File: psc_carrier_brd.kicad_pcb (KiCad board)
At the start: 2 copper layers, 12 parts, among them J1 Conn_01x08_Pin, J2 Conn_01x05_Pin - 3.3v, J3 Conn_01x05_Pin - 5v, J4 6469028-1, J5 39301022, U1 WeMos_D1_mini, U5 OPA2197xDGK

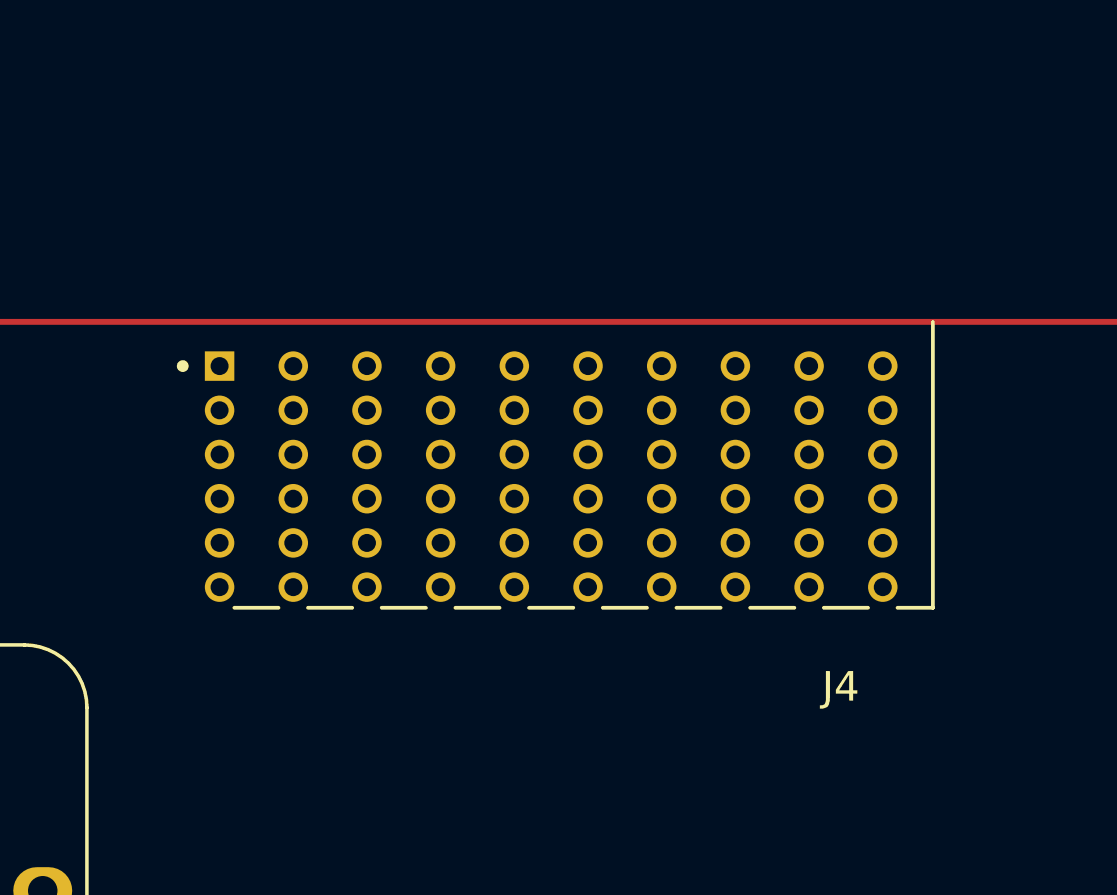
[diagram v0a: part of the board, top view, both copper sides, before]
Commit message: Create 6469028-1 symbol
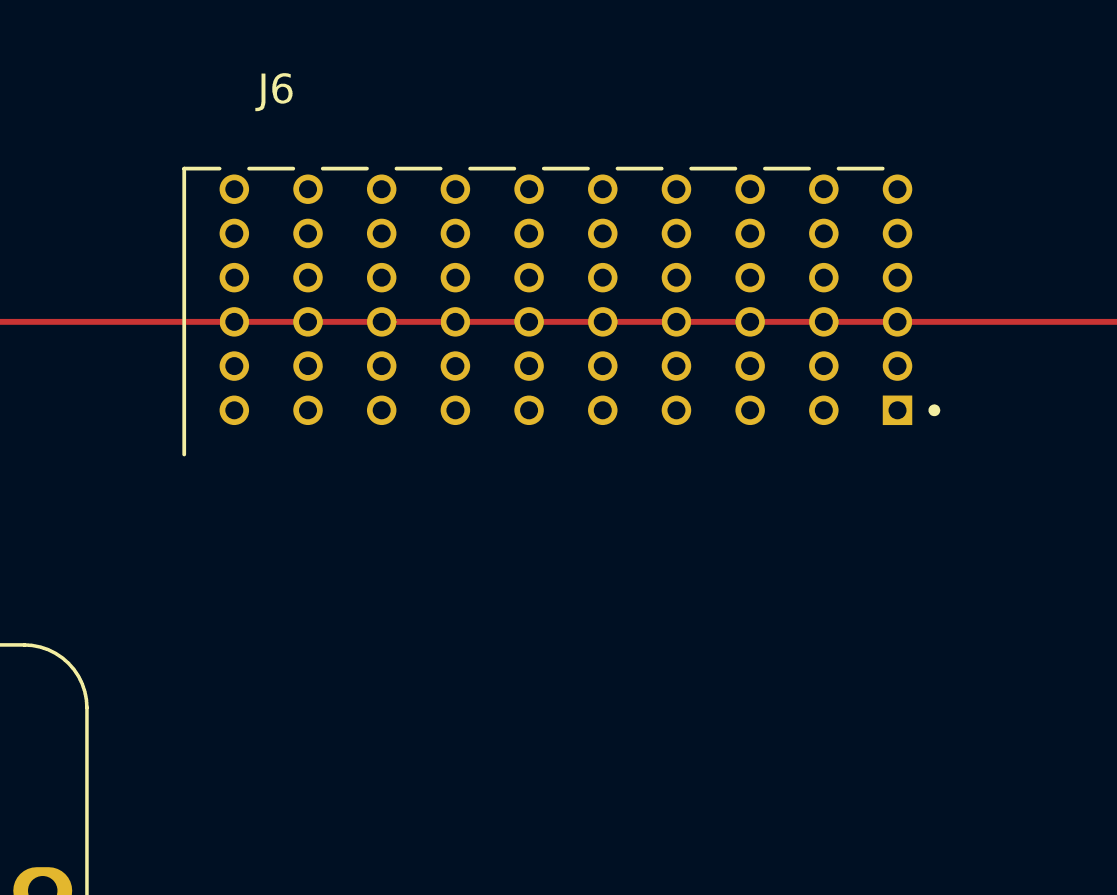
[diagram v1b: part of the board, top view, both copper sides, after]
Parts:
- removed J4: 6469028-1, myparts:TE_6469028-1
- added J6: 6469028-1, myparts:TE_6469028-1, F.Cu at (162.5, 53.0)

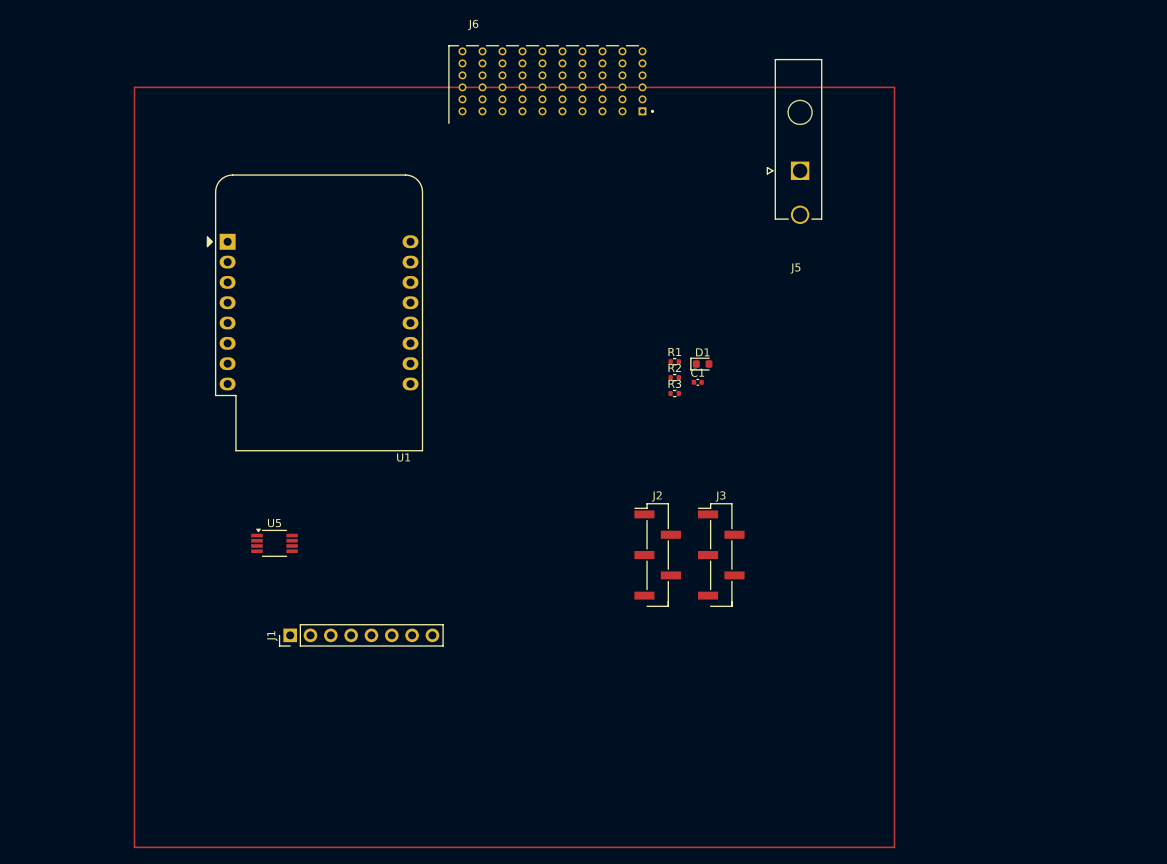
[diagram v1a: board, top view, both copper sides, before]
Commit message: Create custom NSLS2 worksheet
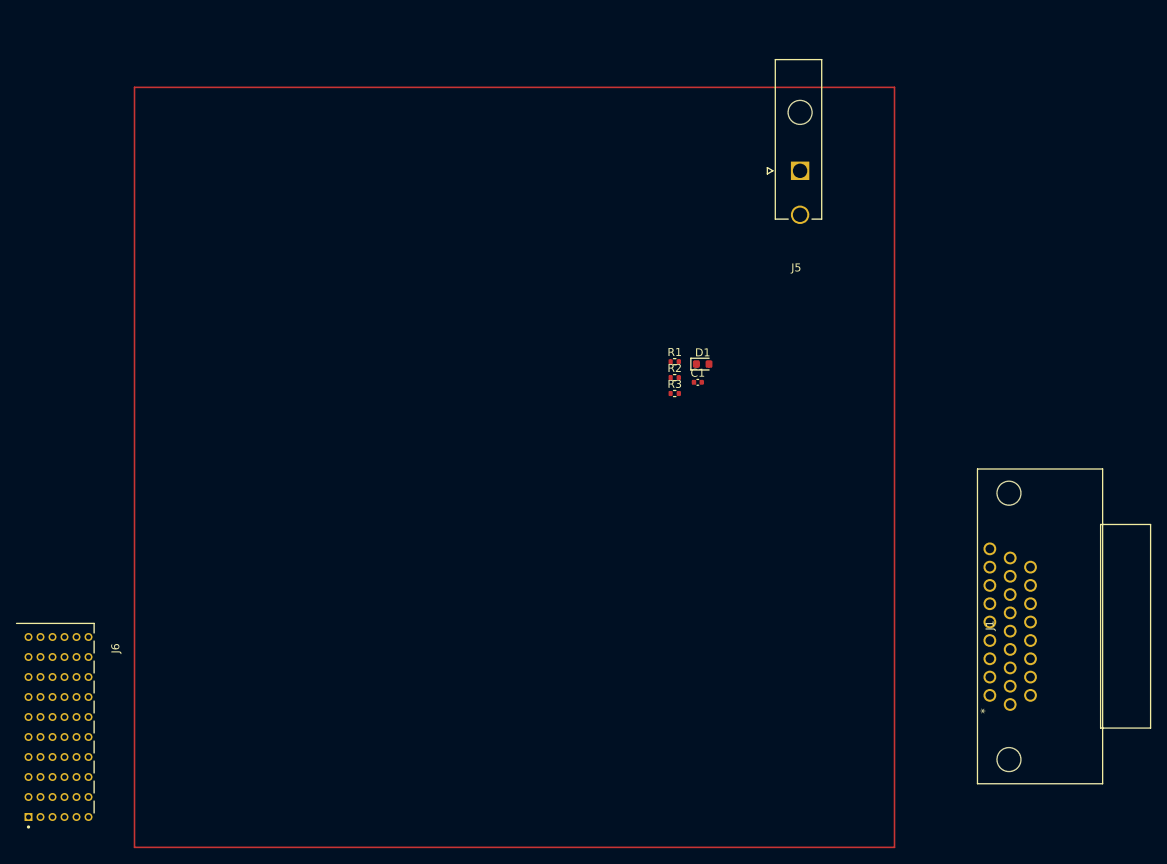
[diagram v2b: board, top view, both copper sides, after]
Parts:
- removed J2: Conn_01x05_Pin - 3.3v, Connector_PinHeader_2.54mm:PinHeader_1x05_P2.54mm_Vertical_SMD_Pin1Left
- removed J3: Conn_01x05_Pin - 5v, Connector_PinHeader_2.54mm:PinHeader_1x05_P2.54mm_Vertical_SMD_Pin1Left
- removed U1: WeMos_D1_mini, Module:WEMOS_D1_mini_light
- removed U5: OPA2197xDGK, Package_SO:VSSOP-8_3.0x3.0mm_P0.65mm
- J1: value Conn_01x08_Pin -> 1731130154; footprint Connector_PinHeader_2.54mm:PinHeader_1x08_P2.54mm_Vertical -> myparts:CONN_F15-26P135G0-5979_MOL
- moved J6 116.9 mm to (85.8, 141.2), turned to -90 degrees
- moved J1 87.8 mm to (205.9, 126.0), turned to -90 degrees
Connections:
- D1 pad 2: Net-(D1-A) -> unconnected-(D1-A-Pad2)
- J1 pad 1: Net-(D1-A) -> unconnected-(J1-Pad1)
- J1 pad 5: Net-(J1-Pin_5) -> unconnected-(J1-Pad5)
- J1 pad 7: Net-(J1-Pin_7) -> unconnected-(J1-Pad7)
- J1 pad 8: Net-(J1-Pin_8) -> unconnected-(J1-Pad8)
- J6 pad A10: (no net) -> unconnected-(J6-PadA10)
- J6 pad A2: (no net) -> unconnected-(J6-PadA2)
- J6 pad A3: (no net) -> unconnected-(J6-PadA3)
- J6 pad A4: (no net) -> unconnected-(J6-PadA4)
- J6 pad A5: (no net) -> unconnected-(J6-PadA5)
- J6 pad A6: (no net) -> unconnected-(J6-PadA6)
- J6 pad A7: (no net) -> unconnected-(J6-PadA7)
- J6 pad A8: (no net) -> unconnected-(J6-PadA8)
- J6 pad A9: (no net) -> unconnected-(J6-PadA9)
- J6 pad B10: (no net) -> unconnected-(J6-PadB10)
- J6 pad B2: (no net) -> unconnected-(J6-PadB2)
- J6 pad B3: (no net) -> unconnected-(J6-PadB3)
- J6 pad B4: (no net) -> unconnected-(J6-PadB4)
- J6 pad B5: (no net) -> unconnected-(J6-PadB5)
- J6 pad B6: (no net) -> unconnected-(J6-PadB6)
- J6 pad B7: (no net) -> unconnected-(J6-PadB7)
- J6 pad B8: (no net) -> unconnected-(J6-PadB8)
- J6 pad B9: (no net) -> unconnected-(J6-PadB9)
- J6 pad BG10: (no net) -> unconnected-(J6-PadBG10)
- J6 pad BG2: (no net) -> unconnected-(J6-PadBG2)
- J6 pad BG3: (no net) -> unconnected-(J6-PadBG3)
- J6 pad BG4: (no net) -> unconnected-(J6-PadBG4)
- J6 pad BG5: (no net) -> unconnected-(J6-PadBG5)
- J6 pad BG6: (no net) -> unconnected-(J6-PadBG6)
- J6 pad BG7: (no net) -> unconnected-(J6-PadBG7)
- J6 pad BG8: (no net) -> unconnected-(J6-PadBG8)
- J6 pad BG9: (no net) -> unconnected-(J6-PadBG9)
- J6 pad C10: (no net) -> unconnected-(J6-PadC10)
- J6 pad C2: (no net) -> unconnected-(J6-PadC2)
- J6 pad C3: (no net) -> unconnected-(J6-PadC3)
- J6 pad C4: (no net) -> unconnected-(J6-PadC4)
- J6 pad C5: (no net) -> unconnected-(J6-PadC5)
- J6 pad C6: (no net) -> unconnected-(J6-PadC6)
- J6 pad C7: (no net) -> unconnected-(J6-PadC7)
- J6 pad C8: (no net) -> unconnected-(J6-PadC8)
- J6 pad C9: (no net) -> unconnected-(J6-PadC9)
- J6 pad D10: (no net) -> unconnected-(J6-PadD10)
- J6 pad D2: (no net) -> unconnected-(J6-PadD2)
- J6 pad D3: (no net) -> unconnected-(J6-PadD3)
- J6 pad D4: (no net) -> unconnected-(J6-PadD4)
- J6 pad D5: (no net) -> unconnected-(J6-PadD5)
- J6 pad D6: (no net) -> unconnected-(J6-PadD6)
- J6 pad D7: (no net) -> unconnected-(J6-PadD7)
- J6 pad D8: (no net) -> unconnected-(J6-PadD8)
- J6 pad D9: (no net) -> unconnected-(J6-PadD9)
- J6 pad DG10: (no net) -> unconnected-(J6-PadDG10)
- J6 pad DG2: (no net) -> unconnected-(J6-PadDG2)
- J6 pad DG3: (no net) -> unconnected-(J6-PadDG3)
- J6 pad DG4: (no net) -> unconnected-(J6-PadDG4)
- J6 pad DG5: (no net) -> unconnected-(J6-PadDG5)
- J6 pad DG6: (no net) -> unconnected-(J6-PadDG6)
- J6 pad DG7: (no net) -> unconnected-(J6-PadDG7)
- J6 pad DG8: (no net) -> unconnected-(J6-PadDG8)
- J6 pad DG9: (no net) -> unconnected-(J6-PadDG9)

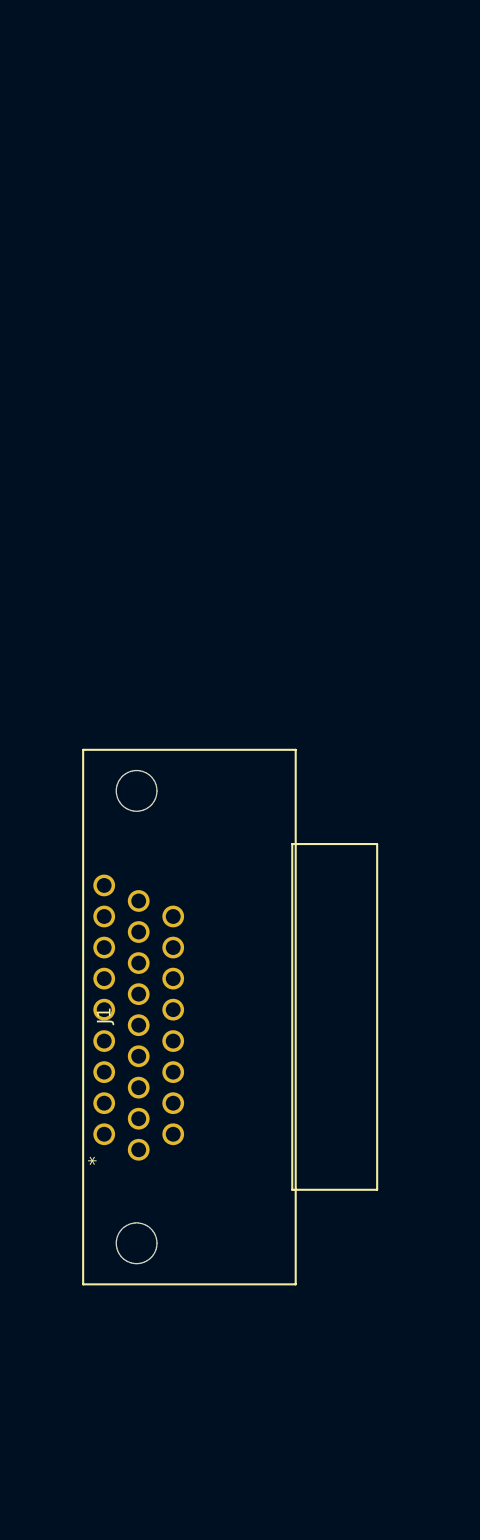
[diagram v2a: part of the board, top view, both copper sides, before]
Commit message: Add footprint for PS connector
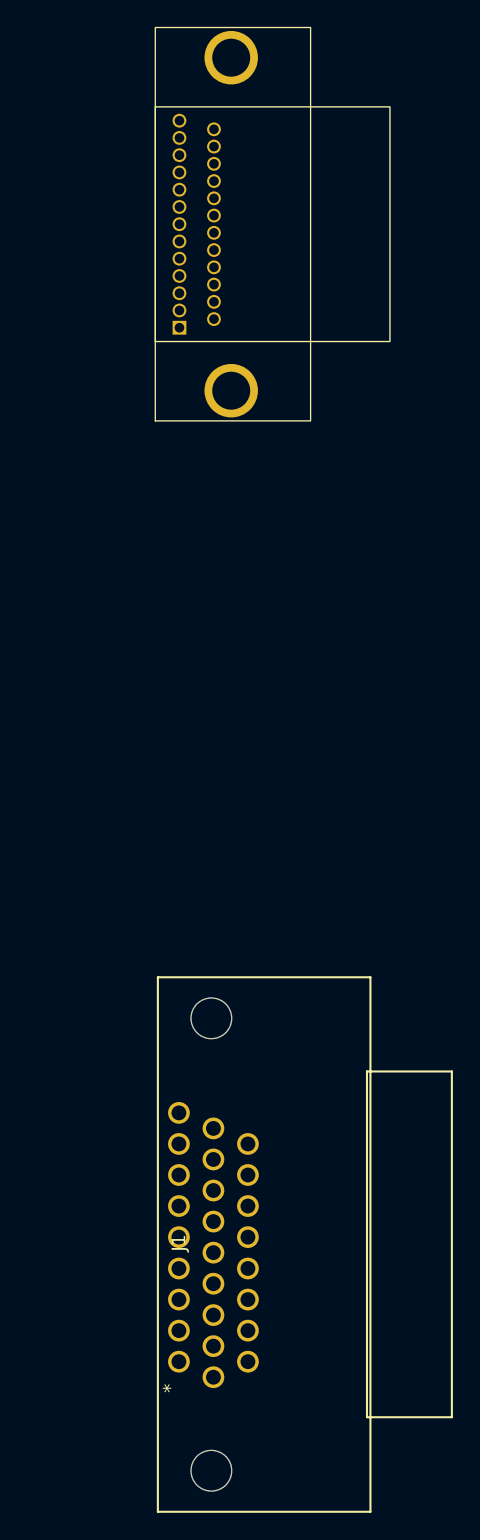
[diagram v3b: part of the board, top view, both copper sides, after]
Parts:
- added J2: 0836149012, myparts:0836149012, F.Cu at (211.5, 59.0)
- moved J1 17.6 mm to (211.4, 142.7)

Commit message: Add board outline
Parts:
- moved J2 135.5 mm to (76.2, 67.3), turned to 180 degrees
- moved J5 126.9 mm to (268.3, 153.7), turned to 90 degrees
- moved J6 87.0 mm to (132.0, 214.9), turned to 0 degrees
- moved J1 81.4 mm to (250.2, 71.1), turned to 0 degrees
- moved C1 50.3 mm to (200.6, 126.3)
- moved R2 50.3 mm to (197.7, 125.8)
- moved R3 50.3 mm to (197.7, 127.8)
- moved D1 50.3 mm to (201.2, 124.1)
- moved R1 50.3 mm to (197.7, 123.8)
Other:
- board outline added: 241.3 x 171.4 mm

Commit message: Upgrade to KiCad 9.  Add all I/O connectors
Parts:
- added J3: 6469028-1, myparts:TE_6469028-1, F.Cu at (142.5, 214.9)
- added J4: 6469028-1, myparts:TE_6469028-1, F.Cu at (193.3, 214.9)
- added J7: 0836149012, myparts:0836149012, F.Cu at (113.0, 66.5)
- added J8: 0836149012, myparts:0836149012, F.Cu at (156.2, 66.5)
- added J9: 0836149012, myparts:0836149012, F.Cu at (199.4, 66.5)
- added MT1: MountingHole_Pad, MountingHole:MountingHole_4.3mm_M4_DIN965_Pad, F.Cu at (44.5, 223.5)
- added MT2: MountingHole_Pad, MountingHole:MountingHole_4.3mm_M4_DIN965_Pad, F.Cu at (87.6, 223.5)
- added MT3: MountingHole_Pad, MountingHole:MountingHole_4.3mm_M4_DIN965_Pad, F.Cu at (226.3, 223.5)
- added MT4: MountingHole_Pad, MountingHole:MountingHole_4.3mm_M4_DIN965_Pad, F.Cu at (275.6, 73.7)
- added MT5: MountingHole_Pad, MountingHole:MountingHole_4.3mm_M4_DIN965_Pad, F.Cu at (275.6, 223.5)
- added MT6: MountingHole_Pad, MountingHole:MountingHole_4.3mm_M4_DIN965_Pad, F.Cu at (44.5, 73.7)
- moved J6 86.7 mm to (218.7, 214.9)
- moved D1 55.5 mm to (256.7, 123.5)
- moved C1 55.5 mm to (256.1, 125.7)
- moved R1 55.5 mm to (253.2, 123.2)
- moved R2 55.5 mm to (253.2, 125.1)
- moved R3 55.5 mm to (253.2, 127.1)
- moved J1 8.15 mm to (258.3, 71.1)
- moved J2 6.40 mm to (69.8, 66.5)
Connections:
- J6 pad BG1: unconnected-(J6-PadBG1) -> GND
- J6 pad BG10: unconnected-(J6-PadBG10) -> GND
- J6 pad BG2: unconnected-(J6-PadBG2) -> GND
- J6 pad BG3: unconnected-(J6-PadBG3) -> GND
- J6 pad BG4: unconnected-(J6-PadBG4) -> GND
- J6 pad BG5: unconnected-(J6-PadBG5) -> GND
- J6 pad BG6: unconnected-(J6-PadBG6) -> GND
- J6 pad BG7: unconnected-(J6-PadBG7) -> GND
- J6 pad BG8: unconnected-(J6-PadBG8) -> GND
- J6 pad BG9: unconnected-(J6-PadBG9) -> GND
- J6 pad DG1: unconnected-(J6-PadDG1) -> GND
- J6 pad DG10: unconnected-(J6-PadDG10) -> GND
- J6 pad DG2: unconnected-(J6-PadDG2) -> GND
- J6 pad DG3: unconnected-(J6-PadDG3) -> GND
- J6 pad DG4: unconnected-(J6-PadDG4) -> GND
- J6 pad DG5: unconnected-(J6-PadDG5) -> GND
- J6 pad DG6: unconnected-(J6-PadDG6) -> GND
- J6 pad DG7: unconnected-(J6-PadDG7) -> GND
- J6 pad DG8: unconnected-(J6-PadDG8) -> GND
- J6 pad DG9: unconnected-(J6-PadDG9) -> GND
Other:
- outline, holes or cut-outs redrawn
